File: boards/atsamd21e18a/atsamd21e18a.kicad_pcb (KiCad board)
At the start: 4 copper layers, 24.1 x 38.1 mm, 26 parts, among them J1 USB_B_Micro, J2 A, J3 B, J4 SWD_1.27, SW1 RESET, U1 AP7361C_SOT-89-5, U2 ATSAMD21E, Y1 <32MHz

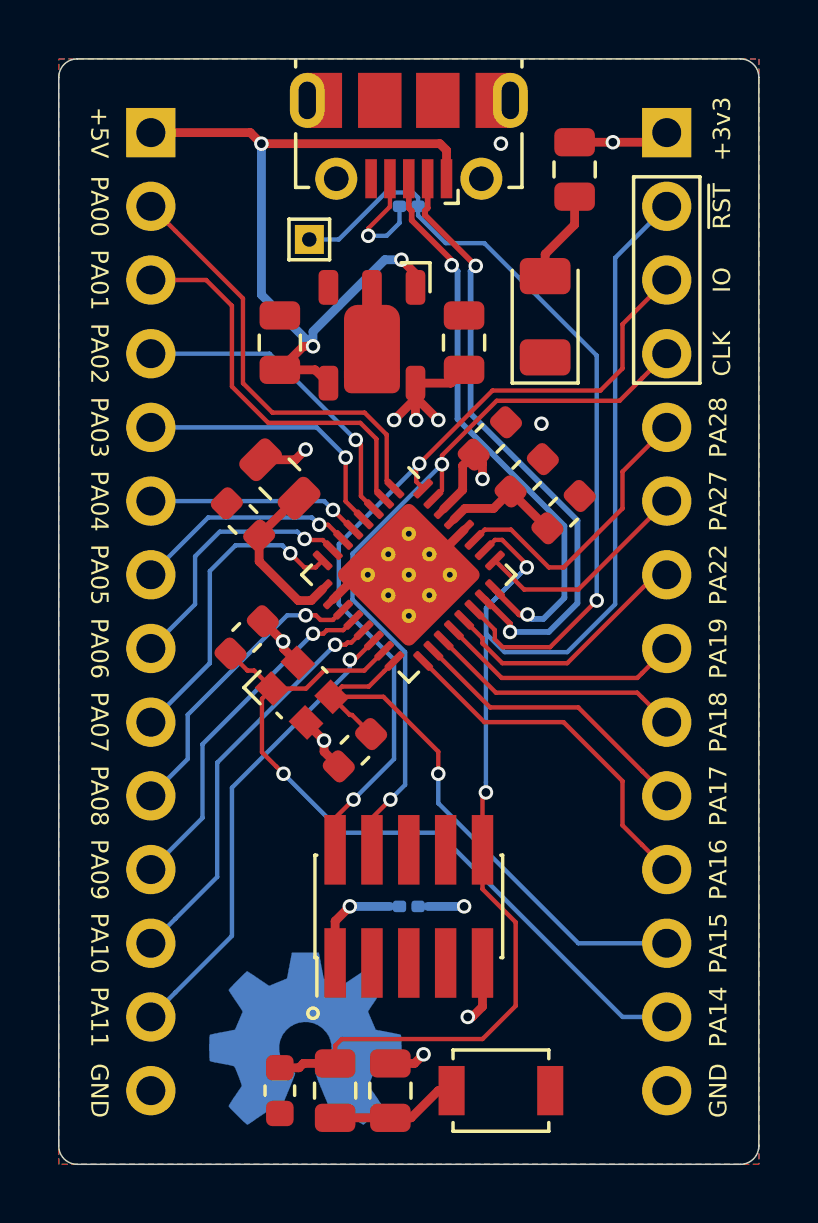
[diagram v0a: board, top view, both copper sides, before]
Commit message: Reduced board width. Reduced size of passives as a result.
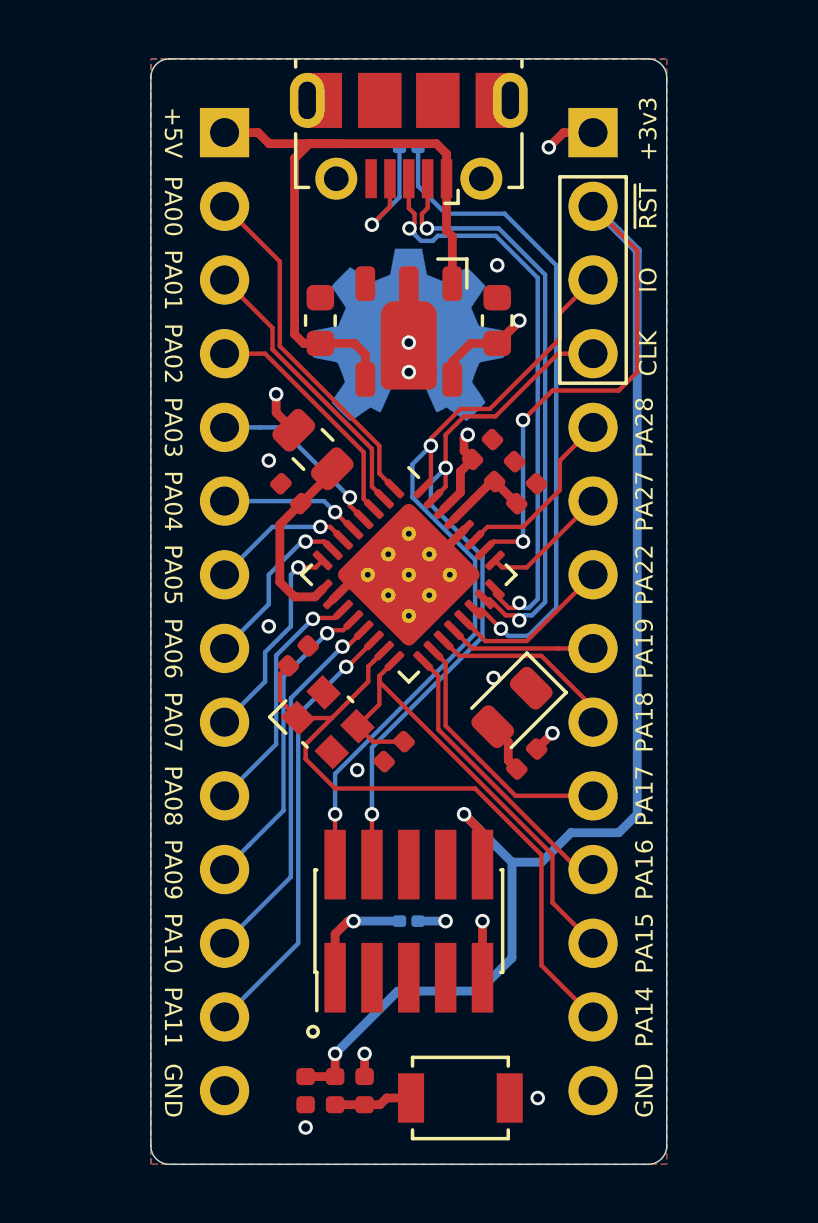
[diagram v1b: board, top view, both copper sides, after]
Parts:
- removed TP1: USB_SOF, TestPoint:TestPoint_THTPad_1.0x1.0mm_Drill0.5mm
- C1, C6: footprint Capacitor_SMD:C_0805_2012Metric -> Capacitor_SMD:C_0603_1608Metric
- C2, C3, C4, C5, C9: footprint Capacitor_SMD:C_0603_1608Metric -> Capacitor_SMD:C_0402_1005Metric
- C7, C8: value 16n -> 18n; footprint Capacitor_SMD:C_0603_1608Metric -> Capacitor_SMD:C_0402_1005Metric
- D1: footprint LED_SMD:LED_1206_3216Metric -> LED_SMD:LED_0805_2012Metric
- R1, R2, R3: footprint Resistor_SMD:R_0805_2012Metric -> Resistor_SMD:R_0402_1005Metric
- moved REF** 24.5 mm to (35.6, 32.4)
- moved R1 20.4 mm to (39.6, 47.0), turned to 225 degrees
- moved D1 13.5 mm to (39.1, 45.2), turned to 225 degrees
- moved J3 2.54 mm to (41.9, 25.4)
- moved J2 2.54 mm to (29.2, 25.4)
- moved JP1 2.03 mm to (35.6, 25.9), turned to 180 degrees
- moved C7 1.89 mm to (31.8, 43.4)
- moved C4 1.88 mm to (31.5, 37.8)
- moved C1 1.59 mm to (32.5, 31.9)
- moved FB1 1.53 mm to (32.3, 36.3)
- moved C2 1.42 mm to (39.6, 37.8)
- moved SW1 1.42 mm to (37.3, 58.7)
- moved C6 1.37 mm to (38.6, 31.9)
- moved Y1 1.35 mm to (32.8, 45.7)
- moved C8 1.35 mm to (35.1, 46.7)
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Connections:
- JP1 pad 1: /USB_SOF -> /PA23
- JP1 pad 2: /PA23 -> /USB_SOF
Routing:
- net /~RESET: track 50.3 -> 60.1 mm, vias 2 -> 4
- net +3V3: track 17.1 -> 12.4 mm, vias 8 -> 7
- net /PA23: track 27.3 -> 22.6 mm
- net +5V: track 28.2 -> 24.0 mm, vias 3 -> 0
- net GND: track 11.6 -> 7.47 mm, vias 4 -> 10
- net /PA01: track 13.9 -> 9.82 mm
- net /PA15: track 20.7 -> 16.9 mm, vias 1 -> 0
- net /PA28: track 10.1 -> 6.29 mm
- net /PA07: track 10.7 -> 7.33 mm
- net /PA19: track 8.44 -> 5.06 mm
- net /PA03: track 9.56 -> 6.27 mm
- net /PA22: track 8.97 -> 5.69 mm
- net /PA06: track 9.17 -> 5.98 mm
- net /PA27: track 7.60 -> 4.43 mm
- net /PA00: track 15.1 -> 12.2 mm
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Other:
- board size 24.1 x 38.1 mm -> 17.8 x 38.1 mm
- net class Default: clearance 0.2 -> 0.1016; trace_width 0.25 -> 0.1016; via_dia 0.8 -> 0.5; via_drill 0.4 -> 0.3
- rule trace_clearance: 0.2 -> 0.1016
- board text added: "atsamd21e18a breakout fourside.io"
- board text removed: "SAMD21E18A Breakout fourside.io"
